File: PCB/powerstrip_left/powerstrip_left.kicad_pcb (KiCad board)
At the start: 2 copper layers, 37 x 100 mm, 0 parts

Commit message: Stripe PCB's
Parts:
- added C1: 100n, Capacitor_SMD:C_0201_0603Metric_Pad0.64x0.40mm_HandSolder, B.Cu at (121.3, 57.0)
- added C10: C_Polarized, Capacitor_THT:CP_Radial_D5.0mm_P2.50mm, F.Cu at (142.8, 133.2)
- added C11: C_Polarized, Capacitor_THT:CP_Radial_D5.0mm_P2.50mm, F.Cu at (139.2, 140.3)
- added C12: 100n, Capacitor_SMD:C_0201_0603Metric_Pad0.64x0.40mm_HandSolder, B.Cu at (116.0, 63.7)
- added C13: 100n, Capacitor_SMD:C_0201_0603Metric_Pad0.64x0.40mm_HandSolder, B.Cu at (118.8, 54.3)
- added C14: 1u, Capacitor_SMD:C_1206_3216Metric_Pad1.33x1.80mm_HandSolder, F.Cu at (123.3, 54.0)
- added C15: 10u Tantal, Capacitor_SMD:C_1206_3216Metric_Pad1.33x1.80mm_HandSolder, F.Cu at (127.3, 47.9)
- added C2: 100n, Capacitor_SMD:C_0201_0603Metric_Pad0.64x0.40mm_HandSolder, B.Cu at (124.3, 48.6)
- added C3: C_Polarized, Capacitor_THT:CP_Radial_D5.0mm_P2.50mm, F.Cu at (139.1, 57.5)
- added C4: C_Polarized, Capacitor_THT:CP_Radial_D5.0mm_P2.50mm, F.Cu at (123.0, 130.5)
- added C5: C_Polarized, Capacitor_THT:CP_Radial_D5.0mm_P2.50mm, F.Cu at (123.2, 136.0)
- added C6: C_Polarized, Capacitor_THT:CP_Radial_D5.0mm_P2.50mm, F.Cu at (132.1, 67.6)
- added C7: C_Polarized, Capacitor_THT:CP_Radial_D5.0mm_P2.50mm, F.Cu at (127.2, 140.3)
- added C8: C_Polarized, Capacitor_THT:CP_Radial_D5.0mm_P2.50mm, F.Cu at (133.2, 140.3)
- added C9: C_Polarized, Capacitor_THT:CP_Radial_D5.0mm_P2.50mm, F.Cu at (132.0, 61.8)
- added IC1: PCA9685PW_Q900,118, Power_Strip_Library:SOP65P640X110-28N, B.Cu at (129.2, 52.9)
- added J1: XT60PW-M, Power_Strip_Library:AMASS_XT60PW-M, B.Cu at (126.7, 96.0)
- added J2: Conn_01x06_Pin, Connector_PinHeader_2.54mm:PinHeader_1x06_P2.54mm_Vertical, F.Cu at (126.6, 129.9)
- added J3: Conn_01x06_Pin, Connector_PinHeader_2.54mm:PinHeader_1x06_P2.54mm_Vertical, F.Cu at (126.6, 132.5)
- added J4: Conn_01x06_Pin, Connector_PinHeader_2.54mm:PinHeader_1x06_P2.54mm_Vertical, F.Cu at (126.6, 135.0)
- added J5: Conn_01x03_Pin, Connector_PinHeader_2.54mm:PinHeader_1x03_P2.54mm_Vertical, F.Cu at (141.2, 67.2)
- added J6: Conn_01x03_Pin, Connector_PinHeader_2.54mm:PinHeader_1x03_P2.54mm_Vertical, F.Cu at (138.6, 67.2)
- added J7: Conn_01x03_Pin, Connector_PinHeader_2.54mm:PinHeader_1x03_P2.54mm_Vertical, F.Cu at (136.1, 67.2)
- added J8: Conn_01x08_Pin, Connector_FFC-FPC:Amphenol_F32Q-1A7x1-11008_1x08-1MP_P0.5mm_Horizontal, B.Cu at (149.3, 59.2)
- added J9: Conn_01x02_Pin, Connector_JST:JST_XH_B2B-XH-AM_1x02_P2.50mm_Vertical, F.Cu at (138.3, 49.1)
- added U1: MUX508IDR, Power_Strip_Library:SOIC127P600X175-16N, B.Cu at (120.2, 64.9)
- added U2: INA181, Package_TO_SOT_SMD:SOT-23-6, B.Cu at (118.7, 56.4)
- added U3: LT1117CST-3.3, PCM_Package_TO_SOT_SMD_AKL:SOT-223-3_TabPin2, F.Cu at (129.2, 52.9)
- added shunt_01: R0.005, Resistor_SMD:R_0201_0603Metric_Pad0.64x0.40mm_HandSolder, B.Cu at (144.0, 67.2)
- added shunt_2: R0.005, Resistor_SMD:R_0201_0603Metric_Pad0.64x0.40mm_HandSolder, B.Cu at (144.0, 64.8)
- added shunt_3: R0.005, Resistor_SMD:R_0201_0603Metric_Pad0.64x0.40mm_HandSolder, B.Cu at (144.1, 62.2)
- added shunt_4: R0.005, Resistor_SMD:R_0201_0603Metric_Pad0.64x0.40mm_HandSolder, B.Cu at (126.6, 126.9)
- added shunt_5: R0.005, Resistor_SMD:R_0201_0603Metric_Pad0.64x0.40mm_HandSolder, B.Cu at (131.7, 126.9)
- added shunt_6: R0.005, Resistor_SMD:R_0201_0603Metric_Pad0.64x0.40mm_HandSolder, B.Cu at (134.2, 126.9)
- added shunt_7: R0.005, Resistor_SMD:R_0201_0603Metric_Pad0.64x0.40mm_HandSolder, B.Cu at (136.8, 126.9)
- added shunt_8: R0.005, Resistor_SMD:R_0201_0603Metric_Pad0.64x0.40mm_HandSolder, B.Cu at (139.3, 126.9)
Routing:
- net PWM_SERVO4: track 0.00 -> 126.9 mm, vias 0 -> 3
- net PWM_SERVO5: track 0.00 -> 122.7 mm, vias 0 -> 3
- net PWM_SERVO6: track 0.00 -> 118.7 mm, vias 0 -> 1
- net PWM_SERVO9: track 0.00 -> 115.7 mm, vias 0 -> 1
- net PWM_SERVO7: track 0.00 -> 114.7 mm, vias 0 -> 1
- net GND_SERVO4: track 0.00 -> 113.5 mm, vias 0 -> 6
- net GND_SERVO6: track 0.00 -> 111.3 mm, vias 0 -> 4
- net PWM_SERVO8: track 0.00 -> 110.8 mm, vias 0 -> 1
- net GND_SERVO7: track 0.00 -> 107.4 mm, vias 0 -> 4
- net GND_SERVO8: track 0.00 -> 103.6 mm, vias 0 -> 4
- net GND_SERVO9: track 0.00 -> 99.8 mm, vias 0 -> 4
- net SDA: track 0.00 -> 59.3 mm, vias 0 -> 4
- net SCL: track 0.00 -> 57.7 mm, vias 0 -> 4
- net ¬EN: track 0.00 -> 54.3 mm, vias 0 -> 4
- net 3.3V: track 0.00 -> 46.2 mm, vias 0 -> 1
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- added copper zone on B.Cu, net GND
- added copper zone on F.Cu, net VCC

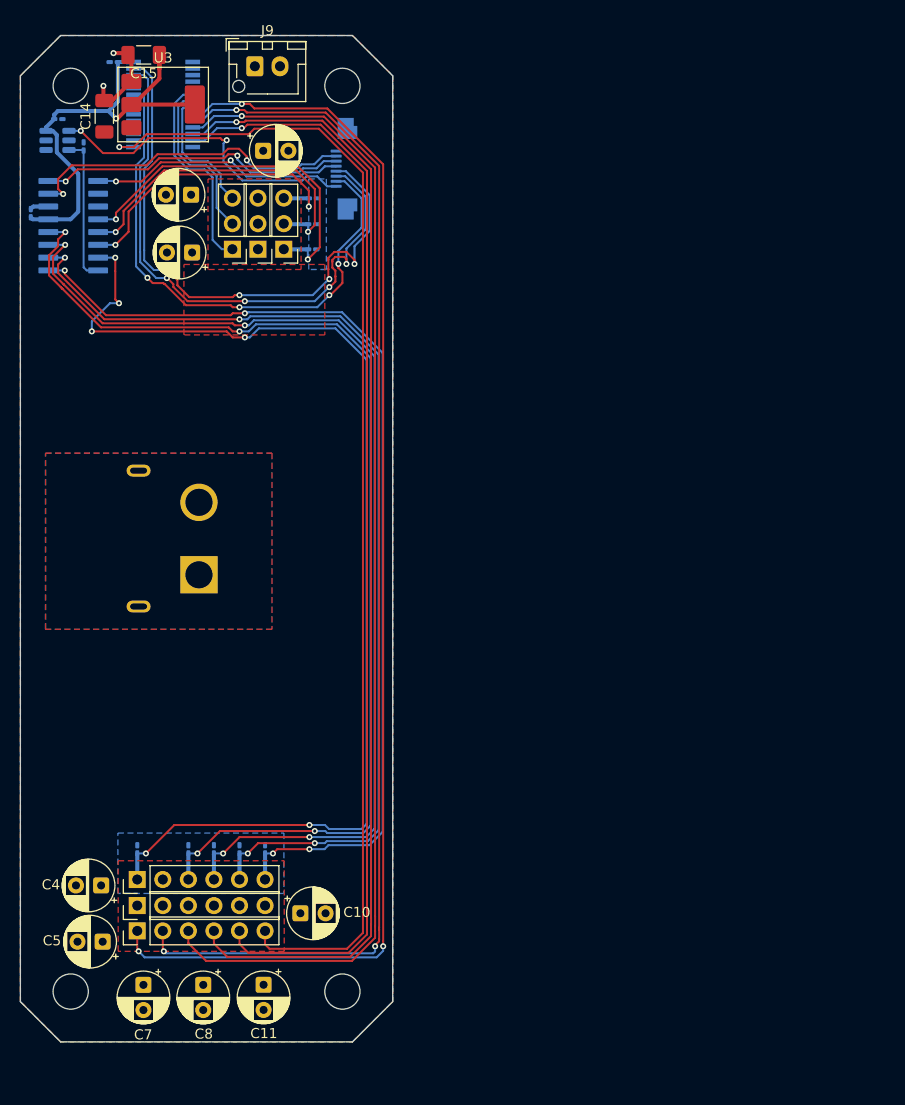
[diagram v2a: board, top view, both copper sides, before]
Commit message: Stop tracking renders folder & final Powerstrip and Mainboard PCB
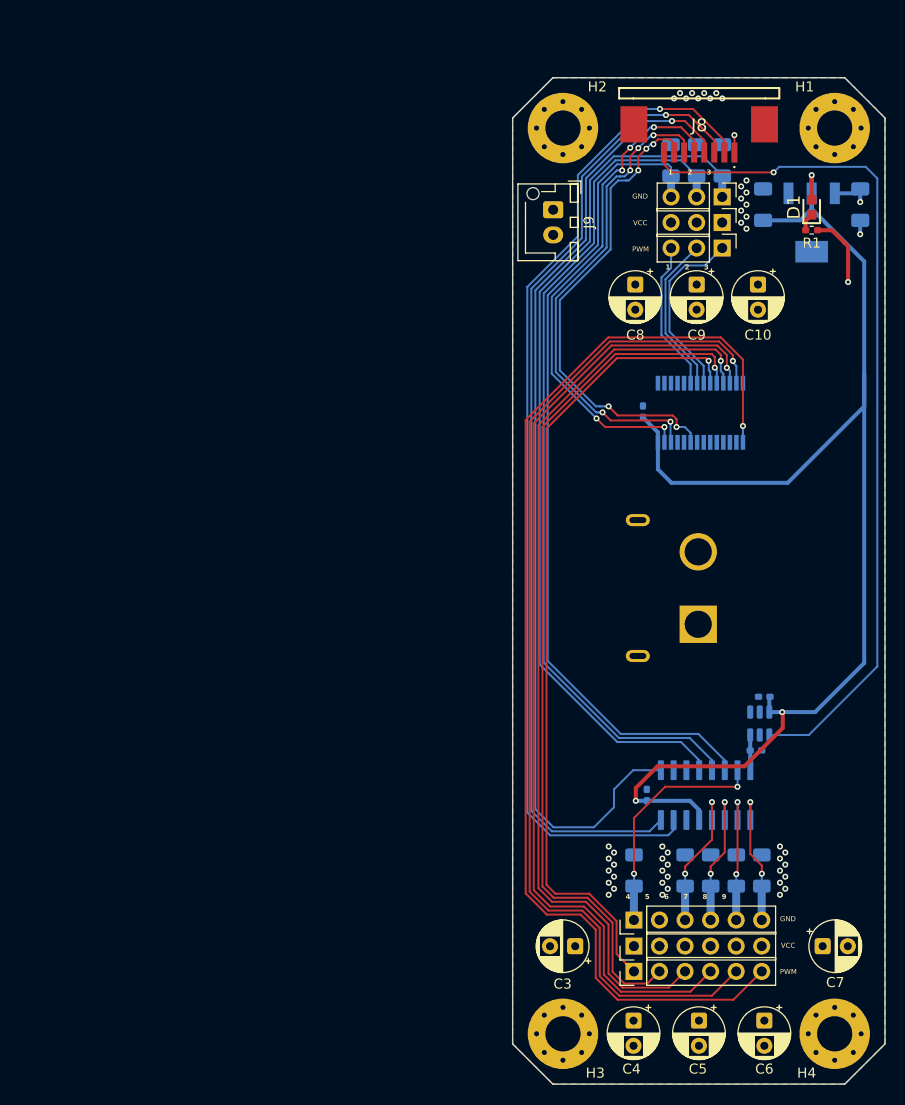
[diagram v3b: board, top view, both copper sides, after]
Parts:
- removed C11: C_Polarized, Capacitor_THT:CP_Radial_D5.0mm_P2.50mm
- added D1: LED, Power_Strip_Library:LEDC1608X70N, F.Cu at (193.6, 63.1)
- added H1: MountingHole_Pad, MountingHole:MountingHole_3.5mm_Pad_Via, F.Cu at (195.9, 55.2)
- added H2: MountingHole_Pad, MountingHole:MountingHole_3.5mm_Pad_Via, F.Cu at (168.9, 55.2)
- added H3: MountingHole_Pad, MountingHole:MountingHole_3.5mm_Pad_Via, F.Cu at (168.9, 145.2)
- added H4: MountingHole_Pad, MountingHole:MountingHole_3.5mm_Pad_Via, F.Cu at (195.9, 145.2)
- added R1: R, Resistor_SMD:R_0402_1005Metric_Pad0.72x0.64mm_HandSolder, F.Cu at (193.6, 65.3)
- C1, C12, C13, C2: footprint Capacitor_SMD:C_0201_0603Metric_Pad0.64x0.40mm_HandSolder -> Capacitor_SMD:C_0402_1005Metric_Pad0.74x0.62mm_HandSolder
- C14, C15: moved to B.Cu
- J8: footprint Connector_FFC-FPC:Amphenol_F32Q-1A7x1-11008_1x08-1MP_P0.5mm_Horizontal -> Power_Strip_Library:17352658; moved to F.Cu
- U3: footprint PCM_Package_TO_SOT_SMD_AKL:SOT-223-3_TabPin2 -> Power_Strip_Library:SOT230P700X180-4N; moved to B.Cu
- shunt_01, shunt_2, shunt_3, shunt_4, shunt_5, shunt_6, shunt_7, shunt_8: footprint Resistor_SMD:R_0201_0603Metric_Pad0.64x0.40mm_HandSolder -> Resistor_SMD:R_1206_3216Metric_Pad1.30x1.75mm_HandSolder
- moved C6 95.2 mm to (188.9, 143.9), turned to -90 degrees
- moved U2 90.7 mm to (188.5, 114.4), turned to 90 degrees
- moved C13 90.6 mm to (188.9, 111.7), turned to 180 degrees
- moved C1 89.8 mm to (188.1, 117.0), turned to 0 degrees
- moved C3 84.9 mm to (170.1, 136.5), turned to 180 degrees
- moved U1 84.6 mm to (183.1, 121.5), turned to -90 degrees
- moved C12 84.2 mm to (177.2, 121.5)
- moved C8 81.8 mm to (176.1, 70.7)
- moved C10 77.3 mm to (188.3, 70.7), turned to -90 degrees
- moved C14 75.6 mm to (198.5, 62.8), turned to -90 degrees
- moved C7 67.6 mm to (194.7, 136.5), turned to 0 degrees
- moved U3 65.5 mm to (193.6, 64.6), turned to -90 degrees
- moved C15 63.3 mm to (188.8, 62.8), turned to 90 degrees
- moved C2 63.0 mm to (176.9, 83.4), turned to 90 degrees
- moved IC1 61.6 mm to (182.6, 83.5), turned to -90 degrees
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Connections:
- net 3.3V renamed +3.3V
- IC1 pad 6: PWM_SERVO1 -> PWM_SERVO3
- IC1 pad 8: PWM_SERVO3 -> PWM_SERVO1
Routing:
- net GND_SERVO6: track 111.3 -> 14.6 mm, vias 4 -> 2
- net GND_SERVO7: track 107.4 -> 14.1 mm, vias 4 -> 2
- net GND_SERVO4: track 113.5 -> 23.4 mm, vias 6 -> 2
- net GND_SERVO8: track 103.6 -> 13.6 mm, vias 4 -> 2
- net +3.3V: track 46.2 -> 133.7 mm, vias 1 -> 3
- net GND_SERVO9: track 99.8 -> 14.0 mm, vias 4 -> 2
- net A0: track 25.7 -> 97.5 mm, vias 2 -> 1
- net A2: track 33.7 -> 101.9 mm, vias 2 -> 1
- net A1: track 31.3 -> 97.2 mm, vias 2 -> 1
- net ADC INPUT: track 32.1 -> 85.5 mm, vias 2 -> 1
- net GND_SERVO3: track 30.6 -> 83.3 mm, vias 2 -> 0
- net GND_SERVO2: track 33.4 -> 85.4 mm, vias 2 -> 0
- net GND_SERVO1: track 36.5 -> 88.0 mm, vias 2 -> 0
- net PWM_SERVO4: track 126.9 -> 80.9 mm, vias 3 -> 1
- net PWM_SERVO5: track 122.7 -> 87.6 mm, vias 3 -> 1
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- added copper zone on In1.Cu, net GND
- added copper zone on In2.Cu, net VCC
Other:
- outline, holes or cut-outs redrawn
- copper layers 2 -> 4
- board text added: "1 2 3"
- board text added: "4 5 6 7 8 9"
- board text added: "GND"
- board text added: "PWM"
- board text added: "S1"
- board text added: "S2"
- board text added: "S3"
- board text added: "S4"
- board text added: "S6"
- board text added: "S7"
- board text added: "S8"
- board text added: "S9"
- board text added: "VCC"
